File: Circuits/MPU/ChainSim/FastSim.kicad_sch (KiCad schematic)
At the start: 12 parts, among them U1 ADA4805-2ARMZ

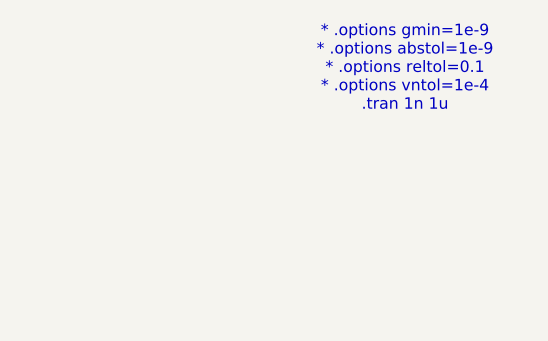
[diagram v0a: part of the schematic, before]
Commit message: try with ngspice
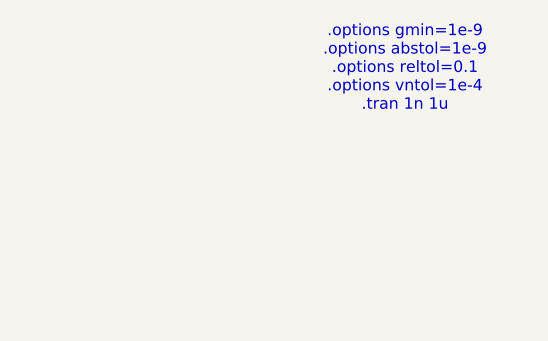
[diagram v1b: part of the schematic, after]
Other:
- note added: ".options gmin=1e-9 .options abstol=1e-9 .options reltol=0.1 .options vntol=1e-4 .tran 1n 1u"
- note removed: "* .options gmin=1e-9 * .options abstol=1e-9 * .options reltol=0.1 * .options vntol=1e-4 .tran 1n 1u"
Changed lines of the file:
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@@
 		)
 	)
-	(text "* .options gmin=1e-9\n* .options abstol=1e-9\n* .options reltol=0.1\n* .options vntol=1e-4\n.tran 1n 1u"
+	(text ".options gmin=1e-9\n.options abstol=1e-9\n.options reltol=0.1\n.options vntol=1e-4\n.tran 1n 1u"
 		(exclude_from_sim no)
 		(at 204.216 30.226 0)
@@
 			)
 		)
-		(property "Sim.Library" "/Users/jpd/Development/QuERI/Circuits/MPU/ChainSim/ADA4805_msop.mod"
+		(property "Sim.Library" "ADA4805_msop.mod"
 			(at 73.66 46.99 0)
 			(effects
@@
 			)
 		)
-		(property "Sim.Name" "ADA4805"
+		(property "Sim.Name" "ADA4805_msop"
 			(at 73.66 46.99 0)
 			(effects
@@
 			)
 		)
-		(property "Sim.Pins" "1=100 2=101 3=102 4=103 5=104 6=106"
+		(property "Sim.Pins" "1=1 2=2 3=3 4=4 5=5 6=6 7=7 8=8"
 			(at 73.66 46.99 0)
 			(effects
@@
 			)
 		)
-		(property "Sim.Library" "/Users/jpd/Development/QuERI/Circuits/MPU/ChainSim/ADA4805_msop.mod"
+		(property "Sim.Library" "ADA4805_msop.mod"
 			(at 132.08 80.01 0)
 			(effects
@@
 			)
 		)
-		(property "Sim.Name" "ADA4805"
+		(property "Sim.Name" "ADA4805_msop"
 			(at 132.08 80.01 0)
 			(effects
@@
 			)
 		)
-		(property "Sim.Pins" "1=100 2=101 3=102 4=103 5=104 6=106"
+		(property "Sim.Pins" "1=1 2=2 3=3 4=4 5=5 6=6 7=7 8=8"
 			(at 132.08 80.01 0)
 			(effects
@@
 			)
 		)
-		(property "Sim.Library" "/Users/jpd/Development/QuERI/Circuits/MPU/ChainSim/ADA4805_msop.mod"
+		(property "Sim.Library" "ADA4805_msop.mod"
 			(at 87.63 127 0)
 			(effects
@@
 			)
 		)
-		(property "Sim.Name" "ADA4805"
+		(property "Sim.Name" "ADA4805_msop"
 			(at 87.63 127 0)
 			(effects
@@
 			)
 		)
-		(property "Sim.Pins" "1=100 2=101 3=102 4=103 5=104 6=106"
+		(property "Sim.Pins" "1=1 2=2 3=3 4=4 5=5 6=6 7=7 8=8"
 			(at 87.63 127 0)
 			(effects

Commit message: almost working with ltspice
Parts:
- added V3: -5V, symbol Simulation_SPICE:VDC
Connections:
- net -5V: now also V3.1
- net GND: now also V3.2
- net IN: now reaches U1.3 (+), V4.1
- net Fast Shaper/IN renamed BUF
